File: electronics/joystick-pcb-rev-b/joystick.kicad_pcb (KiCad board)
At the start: 2 copper layers, 20.6 x 22.4 mm, 7 parts, among them J1 To control board, SW1 KSC221JLFS, SW2 KSC221JLFS, SW3 KSC221JLFS, SW4 KSC221JLFS

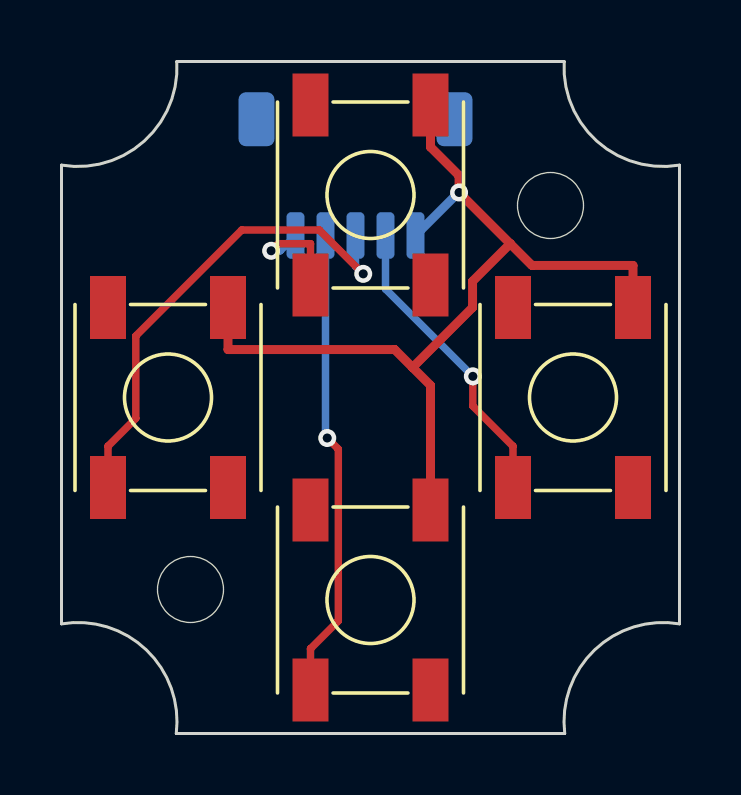
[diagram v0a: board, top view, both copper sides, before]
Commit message: Complete the V0.26 model with cables and keypad
Model the bought cables and their plugs and route them: joystick to
control board round the joystick board's top edge, USB-C board to the
control board in front of its rib, and the pouch's own lead straight
to a top-entry PH socket, with the pouch fitted protection board up
(27 mm of lead instead of a 76 mm run or an extension). The keypad
keys lose their back nubs so the sheet prints flat; the switches sit
in the plate holes and the upper bosses pass through the board. Board
sockets, the TVS and the fuse move to clear the plugs.

Signed-off-by: Marc Cirauqui <marc@tetrate.io>
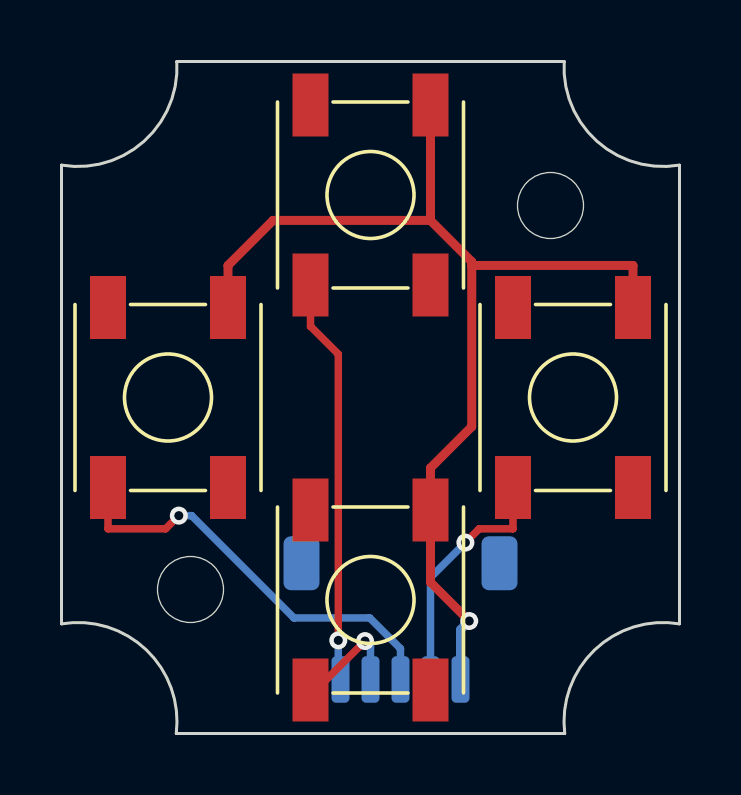
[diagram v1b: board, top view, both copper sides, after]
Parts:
- H1, H2: value M2 standoff -> M2
- moved J1 14.9 mm to (101.0, 107.4)
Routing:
- net /DOWN: track 15.7 -> 3.85 mm
- net /UP: track 3.81 -> 13.6 mm
- net GND: track 31.8 -> 36.5 mm
- net /LEFT: track 16.5 -> 14.2 mm
- net /RIGHT: track 10.2 -> 8.20 mm
